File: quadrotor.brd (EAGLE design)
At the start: 100 x 100 mm, 23 parts, among them T1 AO3400, T2 AO3400, T3 AO3400, T4 AO3400, X1 16MHZ

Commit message: mostly done layout and is routing now
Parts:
- removed C1, C2: 22pF, eagle-ltspice:C0603
- removed JP8: (no value), pinhead:1X06
- added C10, C11, C12, C13, C14, C15, C16, C17, C18, C5, C6, C9: 0.1uF, eagle-ltspice:C0603
- added JP6: (no value), pinhead:1X04
- added LED1: POWER, eagle-ltspice:LED_SML0603
- added R3: 470, eagle-ltspice:R0603
- added SW1: (no value), special:EDG-05
- added U$2: BLT-HC05, quadrotor:BLT-HC05
- added U$3, U$4, U$5, U$6: 720-MSHELL, quadrotor:720MOTOR
- JP5: device pinhead:1X06/90 -> pinhead:1X06
- JP9: device pinhead:1X02/90 -> pinhead:1X02
- X1: device IQD-Frequency-Products:7.5X5-2-PAD -> murata-filter:CSTCR6M
- moved T2 20.7 mm to (-33.0, 33.0), turned to 225 degrees
- moved JP2 19.8 mm to (-35.6, 35.6)
- moved C4 16.9 mm to (8.89, 14.0)
- moved T1 15.3 mm to (-29.2, -29.2), turned to 315 degrees
- moved JP1 14.4 mm to (-31.8, -31.8)
- moved JP4 14.4 mm to (31.8, -31.8)
- moved T3 14.4 mm to (27.9, 27.9), turned to 135 degrees
- moved T4 14.4 mm to (29.2, -29.2), turned to 45 degrees
- moved JP5 13.0 mm to (14.0, -9.53)
- moved JP3 12.6 mm to (30.5, 30.5)
- moved U$1 12.3 mm to (1.91, 15.2), turned to 0 degrees
- moved C8 12.0 mm to (6.35, 14.0)
- moved R1 11.7 mm to (0.00, 14.0), turned to 90 degrees
- moved C7 9.25 mm to (-2.54, 14.0), turned to 270 degrees
- moved JP9 8.98 mm to (-14.0, -3.81)
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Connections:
- removed net PD0: ATMEGA328P.30, JP8.4
- removed net PD1: ATMEGA328P.31, JP8.5
- new net N$11: SW1.8, U$2.VCC
- new net N$12: SW1.7, U$2.TX
- new net N$13: SW1.6, U$2.RX
- new net N$14: JP9.1, SW1.1
- new net N$15: C12.2, C17.1, U$4.SHELL
- new net N$16: C13.2, C16.1, U$6.SHELL
- new net N$3: C14.2, C15.1, U$5.SHELL
- new net N$5: C11.2, C18.1, U$3.SHELL
- new net N$7: SW1.9, U$2.EN
- new net N$8: LED1.A, R3.1
- new net PD0/RX: ATMEGA328P.30, JP6.3, SW1.4
- new net PD1/TX: ATMEGA328P.31, JP6.2, SW1.5
- net GND: now also C11.1, C12.1, C13.1, C14.1, JP5.6, JP6.4, LED1.C, U$2.GND, X1.2; no longer C1.1, C2.1, JP5.5, JP8.3
- net MISO: now also JP5.4; no longer JP5.3
- net MOSI: now also JP5.5; no longer JP5.4
- net N$1: no longer C2.2
- net N$10: now also C9.1
- net N$2: now also X1.3; no longer C1.2, X1.2
- net N$4: now also C5.1
- net N$6: now also C6.1
- net N$9: now also C10.1
- net PD2: now also U$2.STATE; no longer JP8.6
- net RESET: now also JP5.2; no longer JP5.1
- net SCK: now also JP5.3; no longer JP5.2
- net VCC: now also SW1.2, SW1.3; no longer JP8.1, JP8.2
- net VIN: now also C10.2, C15.2, C16.2, C17.2, C18.2, C5.2, C6.2, C9.2, JP5.1, JP6.1, R3.2, SW1.10; no longer JP5.6, JP9.1
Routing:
- net N$5: track 141.4 -> 0.00 mm
- net N$3: track 141.4 -> 0.00 mm
- net M2: track 0.00 -> 69.7 mm
- net M3: track 0.00 -> 69.2 mm, vias 0 -> 2
- net M1: track 0.00 -> 38.8 mm
- net GND: track 77.2 -> 42.0 mm
- net M4: track 0.00 -> 33.7 mm
- net PD0/RX: track 0.00 -> 31.2 mm, vias 0 -> 1
- net VCC: track 52.7 -> 22.6 mm
- net N$14: track 0.00 -> 28.8 mm
- net PD1/TX: track 0.00 -> 27.3 mm, vias 0 -> 1
- net N$13: track 0.00 -> 21.9 mm
- net N$12: track 0.00 -> 17.6 mm
- net N$1: track 16.5 -> 2.83 mm
- net RESET: track 20.1 -> 33.6 mm, vias 0 -> 1
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- added copper zone on layer 1, net GND
- added copper zone on layer 16, net GND
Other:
- board size 100 x 100 mm -> 111 x 111 mm

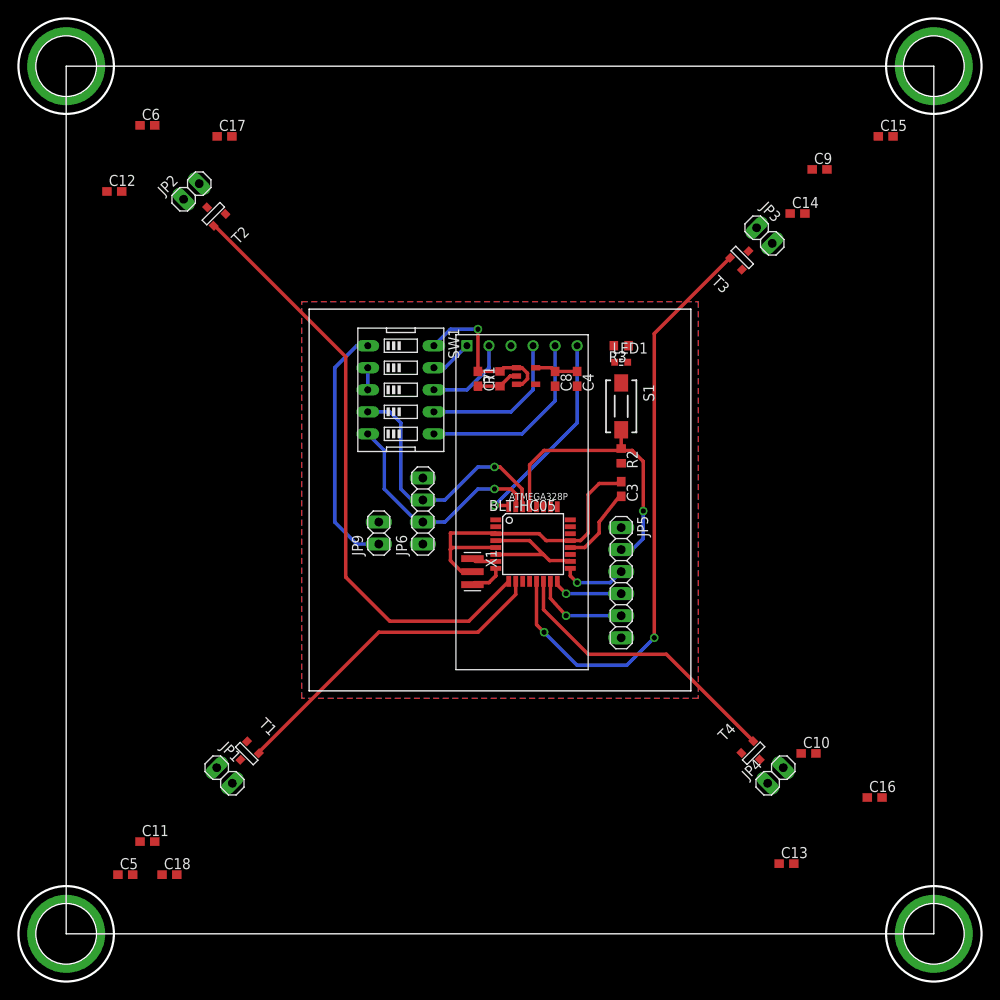
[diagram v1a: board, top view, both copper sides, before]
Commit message: basically done pcb layout
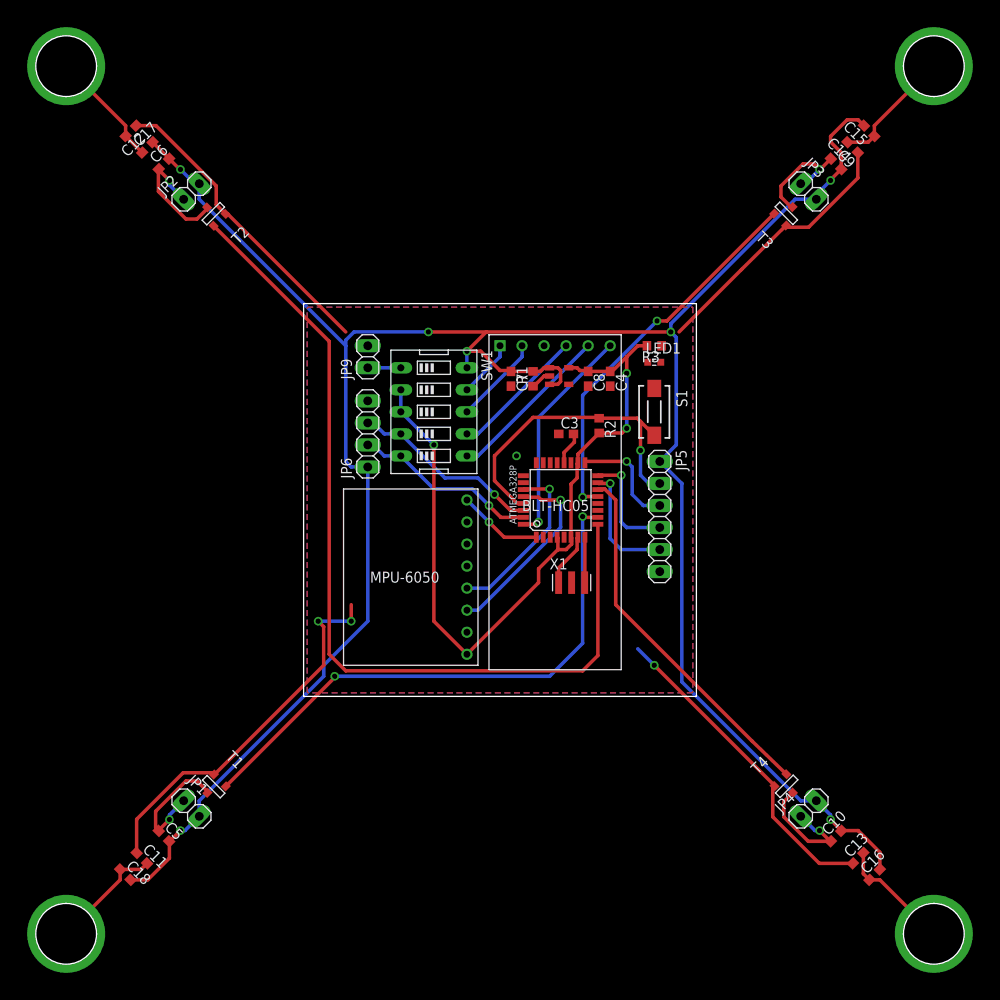
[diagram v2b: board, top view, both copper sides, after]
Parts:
- added U$7: MPU-6050, quadrotor:MPU-6050
- moved JP9 20.4 mm to (-15.2, 16.5)
- moved X1 11.5 mm to (8.26, -9.53), turned to 0 degrees
- moved JP6 10.9 mm to (-15.2, 7.62)
- moved C10 10.0 mm to (38.7, -38.7), turned to 45 degrees
- moved C14 9.92 mm to (40.6, 40.6), turned to 135 degrees
- moved C17 8.98 mm to (-40.6, 40.6), turned to 45 degrees
- moved C3 8.98 mm to (7.62, 7.62), turned to 0 degrees
- moved C16 8.89 mm to (43.2, -43.2), turned to 45 degrees
- moved JP5 8.82 mm to (18.4, -1.91)
- moved C13 8.28 mm to (41.3, -41.3), turned to 45 degrees
- moved C12 7.24 mm to (-42.5, 42.5), turned to 225 degrees
- moved JP3 7.18 mm to (35.6, 35.6)
- moved T3 7.18 mm to (33.0, 33.0)
- moved C5 6.29 mm to (-38.7, -38.7), turned to 315 degrees
- moved ATMEGA328P 5.99 mm to (6.99, 0.00), turned to 90 degrees
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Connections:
- net GND: now also U$7.GND
- net PC4: now also U$7.SDA
- net PC5: now also U$7.SCL
- net PD3: now also U$7.INT
- net VCC: now also R3.2, U$7.VCC
- net VIN: no longer R3.2
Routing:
- net VIN: track 19.1 -> 281.1 mm, vias 1 -> 7
- net GND: track 42.0 -> 150.2 mm, vias 0 -> 4
- net VCC: track 22.6 -> 89.6 mm, vias 0 -> 3
- net M2: track 69.7 -> 102.5 mm
- net M1: track 38.8 -> 64.4 mm, vias 0 -> 2
- net N$14: track 28.8 -> 3.81 mm
- net M3: track 69.2 -> 44.3 mm
- net PC5: track 0.00 -> 22.4 mm, vias 0 -> 1
- net PC4: track 0.00 -> 19.9 mm, vias 0 -> 1
- net N$4: track 0.00 -> 15.1 mm, vias 0 -> 1
- net N$6: track 0.00 -> 14.8 mm, vias 0 -> 1
- net N$9: track 0.00 -> 14.5 mm, vias 0 -> 1
- net N$3: track 0.00 -> 14.3 mm
- net N$15: track 0.00 -> 13.6 mm
- net N$10: track 0.00 -> 13.5 mm, vias 0 -> 1
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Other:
- board size 111 x 111 mm -> 45.3 x 45.3 mm

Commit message: basically done v1 brd
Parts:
- moved C16 3.59 mm to (40.6, -40.6)
- moved C18 3.59 mm to (-40.6, -40.6)
- moved C14 2.69 mm to (42.5, 42.5)
- moved C15 2.69 mm to (40.6, 40.6), turned to 315 degrees
- moved C11 1.80 mm to (-42.5, -42.5)
- moved C13 1.80 mm to (42.5, -42.5)
- moved JP6 1.27 mm to (-15.2, 6.35)
- moved C3 0.95 mm to (6.67, 7.62)
- moved U$3 0.23 mm to (-50.2, -50.2)
- moved U$4 0.23 mm to (-50.2, 50.2)
- moved U$5 0.23 mm to (50.2, 50.2)
- moved U$6 0.23 mm to (50.2, -50.2)
- renumbered LED1 to POW
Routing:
- net GND: track 150.2 -> 36.9 mm, vias 4 -> 1
- net VIN: track 281.1 -> 262.3 mm, vias 7 -> 2
- net VCC: track 89.6 -> 102.5 mm, vias 3 -> 2
- net N$4: track 15.1 -> 7.78 mm, vias 1 -> 0
- net N$6: track 14.8 -> 7.76 mm, vias 1 -> 0
- net N$9: track 14.5 -> 7.78 mm, vias 1 -> 0
- net N$10: track 13.5 -> 7.76 mm, vias 1 -> 0
- net N$8: track 0.00 -> 1.95 mm
- net M3: track 44.3 -> 46.1 mm
- net N$16: track 13.4 -> 14.5 mm
- net N$5: track 13.4 -> 14.5 mm
- net M2: track 102.5 -> 101.4 mm
- net RESET: track 37.2 -> 38.1 mm, vias 1 -> 0
- net PD1/TX: track 21.4 -> 20.9 mm, vias 1 -> 0
- net PD0/RX: track 22.1 -> 21.6 mm, vias 1 -> 0
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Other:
- board size 45.3 x 45.3 mm -> 113 x 113 mm
